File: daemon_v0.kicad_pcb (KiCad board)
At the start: 4 copper layers, 85.6 x 54 mm, 164 parts, among them J1 BATTERY JST, J10 WAGO 24V I/O, J11 AUX GPIO, J12 RADXA 40-PIN HEADER, J13 TRRS AUDIO, J14 SPEAKER, J2 USB-A ① (MALE), J3 USB-A ②, J4 USB-A ③, J5 SCREEN 8-PIN, J6 JOYSTICK 5-PIN, J7 PWR HDR, J8 USB-C GOOBAY, J9 RJ45 ETHERNET, Q1 PNP BC857, Q2 PMOS BSS84, Q3 NMOS 2N7002, Q4 IR DRIVE AO3400A, SW1 POWER BUTTON, U1 PMIC IP5328P, U10 ETH RTL8152B, U11 ISO ISO1212, U12 AMP MAX98357A, U13 MIC INMP441, U2 LDO 3.3V AP2112K, U3 HEARTBEAT NE555, U4 USB HUB SL2.1A, U5 STINGER 1 SY6280, U6 STINGER 2 SY6280, U7 STINGER 3 SY6280, U8 ADC ADS1015, U9 RF CC1101, Y1 12MHz, Y2 26MHz, Y3 25MHz

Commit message: feat: layout-ready board with Radxa reference, placement guide, and component grid
- Radxa Zero 3W outline drawn on User.Drawings (connectors, GPIO header, mounting holes)
- 55 key components staged in labeled grid (right of board) — drag onto board
- 109 passives hidden below board — follow parent ICs later
- docs/PLACEMENT_GUIDE.md: gamified step-by-step placement with separation rules
- docs/PLACEMENT_CONSTRAINTS.md: detailed A/B/C component classification
- docs/RADXA_REFERENCE.md: GPIO mapping, alignment, keep-out zones

Co-Authored-By: Claude Opus 4.6 <noreply@anthropic.com>
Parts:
- AE1: value 915MHz ANTENNA -> ANTENNA 915MHz
- C12: value 100u -> 100µF ELEC TIMER
- C7: value 100u -> 100µF TANT POWER TANK
- D1: value SS14 -> SS14 DIODE A
- D2: value SS14 -> SS14 DIODE B
- D3: value LED① -> WS2812B ①
- D4: value LED② -> WS2812B ②
- D5: value LED③ -> WS2812B ③
- D6: value LED④ -> WS2812B ④
- D7: value IR LED -> IR LED VSMB294008
- D8: value VCAN26A2 -> TVS ① VCAN26A2
- D9: value VCAN26A2 -> TVS ② VCAN26A2
- F1: value 60R -> PTC FUSE ①
- F2: value 60R -> PTC FUSE ②
- J12: value RADXA 40-PIN HEADER -> RADXA 40-PIN HDR
- J14: value SPEAKER -> SPEAKER JST
- J2: value USB-A ① (MALE) -> USB-A ① MALE
- J9: value RJ45 ETHERNET -> RJ45 MAGJACK
- L1: value 4.7µH BOOST -> 4.7µH BOOST IND
- Q1: value PNP BC857 -> BC857 PNP
- Q2: value PMOS BSS84 -> BSS84 PMOS
- Q3: value NMOS 2N7002 -> 2N7002 NMOS
- Q4: value IR DRIVE AO3400A -> AO3400A IR DRIVE
- TH1: value 10k -> NTC 10K (near U1!)
- U1: value PMIC IP5328P -> IP5328P PMIC
- U10: value ETH RTL8152B -> RTL8152B ETH PHY
- U11: value ISO ISO1212 -> ISO1212
- U12: value AMP MAX98357A -> MAX98357A AMP
- U13: value MIC INMP441 -> INMP441 MEMS MIC
- U2: value LDO 3.3V AP2112K -> AP2112K 3.3V LDO
- U3: value HEARTBEAT NE555 -> NE555 HEARTBEAT
- U4: value USB HUB SL2.1A -> SL2.1A USB HUB
- U5: value STINGER 1 SY6280 -> SY6280 ① (near J2)
- U6: value STINGER 2 SY6280 -> SY6280 ② (near J3)
- U7: value STINGER 3 SY6280 -> SY6280 ③ (near J4)
- U8: value ADC ADS1015 -> ADS1015 JOY ADC
- U9: value RF CC1101 -> CC1101 RF XCVR
- Y1: value 12MHz -> 12MHz XTAL (near U4)
- Y2: value 26MHz -> 26MHz XTAL (near U9)
- Y3: value 25MHz -> 25MHz XTAL (near U10)
- moved TP1 486.4 mm to (490.6, 95.0)
- moved TP2 484.1 mm to (490.6, 113.0)
- moved TP3 482.5 mm to (490.6, 131.0)
- moved TP4 481.7 mm to (490.6, 149.0)
- moved Q4 468.7 mm to (470.6, 149.0)
- moved Q3 466.6 mm to (470.6, 131.0)
- moved Q2 462.5 mm to (470.6, 113.0)
- moved Q1 461.0 mm to (470.6, 95.0)
- moved U8 447.3 mm to (450.6, 95.0)
- moved D6 435.2 mm to (430.6, 149.0)
- moved U3 433.0 mm to (450.6, 113.0)
- moved D5 430.8 mm to (430.6, 131.0)
- moved D4 427.0 mm to (430.6, 113.0)
- moved D3 424.2 mm to (430.6, 95.0)
- moved SW1 423.2 mm to (450.6, 131.0)
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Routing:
- removed copper zone on B.Cu, net (none)
- removed copper zone on F.Cu, net (none)
- removed copper zone on In1.Cu, net (none)
- removed copper zone on In2.Cu, net (none)
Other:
- board text added: "1"
- board text added: "40"
- board text added: "40-PIN GPIO HEADER"
- board text added: "54.0 mm"
- board text added: "Inductor↔XTALs ≥15mm | Antenna keepout 5mm | MagJack↔USB-C ≥15mm"
- board text added: "M2.5"
- board text added: "RADXA ZERO 3W (underneath)"
- board text added: "RULES: Power↔RF ≥20mm | Inductor↔RF ≥25mm | XTAL_26↔XTAL_25 ≥10mm"
- board text added: "SD"
- board text added: "SECONDARY COMPONENTS (109 passives) — don't touch, they follow their parent IC"
- board text added: "USB-C HOST"
- board text added: "USB-C OTG/PWR"
- board text added: "WiFi U.FL"
- board text added: "µHDMI"
- board text added: "← 85.6 mm →"
- board text added: "⚙️ INDUSTRIAL ISO"
- board text added: "⚠ NO TALL PARTS ON B.Cu IN THIS ZONE"
- board text added: "⚡ POWER"
- board text added: "🌐 ETHERNET"
- board text added: "🎮 CONTROL"
- board text added: "💡 LEDs + IR"
- board text added: "📍 TEST POINTS"
- board text added: "📡 RF (keep away from power!)"
- board text added: "🔀 USB HUB"
- board text added: "🔊 AUDIO"
- board text added: "🔌 CONNECTORS"
- board text added: "🔌 STINGER SWITCHES"
- board text added: "🔧 TRANSISTORS"

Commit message: fix: resolve hardware review blocker + warnings
BLOCKER B-1 FIXED:
- NE555 DIP-8 → NE555DR SOIC-8 (turnkey SMT compatible)
- 100µF electrolytic (THT, 8mm tall) → 100µF tantalum Case-D (SMD, 2.8mm)
- Eliminates all through-hole dependencies except RJ45 MagJack
- Resolves Z-height collision risk with Radxa stack

WARNING W-5 FIXED:
- C_TANT voltage rating 6.3V → 10V (2x derating on 5V rail)

HARDWARE REVIEW added (docs/HARDWARE_REVIEW.md):
- 1 blocker (now fixed), 11 warnings (quantified), 15 verified stable
- Power system, RF, audio, USB hub, Ethernet all verified stable
- Key remaining risks: WS2812B level (firmware open-drain), LDO thermal margin

Co-Authored-By: Claude Opus 4.6 <noreply@anthropic.com>
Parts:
- C12: footprint CP_Radial_D6.3mm_P2.50mm -> CP_EIA-7343-31_Kemet-D
- U3: footprint DIP-8_W7.62mm -> SOIC-8_3.9x4.9mm_P1.27mm

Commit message: fix: 40-pin header to female socket, add mic power LED, edge-mount power button
ECO #2026-03-HWR fixes:
- J12: PinHeader_2x20 → PinSocket_2x20 (female socket mates with Radxa male pins)
- SW1: PTS645 top-press → Alps SKRTLAE010 right-angle (flush with board edge)
- Added red 0402 LED + 1k resistor on INMP441 VDD (hardware mic-active indicator)
- Total components: 164 → 166 (mic LED + resistor added)
- All 164 tests pass

Co-Authored-By: Claude Opus 4.6 <noreply@anthropic.com>
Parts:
- added D12: RED_0402, LED_0402_1005Metric, F.Cu at (110.0, 184.0)
- added R45: 1k, R_0402_1005Metric, F.Cu at (125.0, 194.0)
- J12: footprint PinHeader_2x20_P2.54mm_Vertical -> PinSocket_2x20_P2.54mm_Vertical
- SW1: footprint SW_SPST_PTS645 -> SW_Push_1P1T-MP_NO_Horizontal_Alps_SKRTLAE010
- moved R22 95.1 mm to (100.0, 189.0)
- moved R40 95.1 mm to (100.0, 194.0)
- moved R5 10.0 mm to (130.0, 194.0)
- moved R6 10.0 mm to (135.0, 194.0)
- moved R7 10.0 mm to (140.0, 194.0)
- moved R8 10.0 mm to (145.0, 194.0)
- moved R9 10.0 mm to (150.0, 194.0)
- moved FB1 5.00 mm to (115.0, 184.0)
- moved FB2 5.00 mm to (120.0, 184.0)
- moved L2 5.00 mm to (125.0, 184.0)
- moved R1 5.00 mm to (130.0, 184.0)
- moved R10 5.00 mm to (135.0, 184.0)
- moved R11 5.00 mm to (140.0, 184.0)
- moved R12 5.00 mm to (145.0, 184.0)
- moved R13 5.00 mm to (150.0, 184.0)
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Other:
- board text added: "SECONDARY COMPONENTS (111 passives) — don't touch, they follow their parent IC"
- board text removed: "SECONDARY COMPONENTS (109 passives) — don't touch, they follow their parent IC"

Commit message: fix: netlist pad numbering + KiCad import with full net assignments
The netlist was outputting pin NAMES (CC1, VDD, EPAD, D+, etc.) but
KiCad footprints use pad NUMBERS (1, 2, 3...). Every IC had zero net
connections in KiCad because "CC1" != pad "2".

Added PIN_MAPS dict to gen_golden_netlist.py mapping pin names to KiCad
pad numbers for all 20+ IC/connector types (IP5328P QFN-40, SL2.1A,
RTL8152B, MAX98357A, CC1101, ISO1212, PCF8574, NE555, AP2112K, SY6280,
USB-C plug/receptacle, USB-A, TRRS jack, WS2812B, LEDs, MOSFETs, etc.)

Updated import_netlist.py to use .net file pad assignments directly
instead of trying to match pin names. Result: 802/802 pad-net
connections assigned (was 0).

Co-Authored-By: Claude Opus 4.6 (1M context) <noreply@anthropic.com>
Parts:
- removed AE1: ANTENNA 915MHz, Antenna_Chip_Johanson_0915AT43A0026
- removed D12: RED_0402, LED_0402_1005Metric
- removed J5: SCREEN 8-PIN, PinHeader_1x08_P2.54mm_Vertical
- removed TH1: NTC 10K (near U1!), R_0402_1005Metric
- added ANT1: 0915AT43A0026, Antenna_Chip_Johanson_0915AT43A0026, F.Cu at (280.0, 180.0)
- added BAT1: Li-ion, JST_PH_S2B-PH-K_1x02_P2.00mm_Horizontal, F.Cu at (220.0, 100.0)
- added C100: 100n, C_0402_1005Metric, F.Cu at (264.0, 468.0)
- added C101: 100n, C_0402_1005Metric, F.Cu at (272.0, 468.0)
- added C102: 100n, C_0402_1005Metric, F.Cu at (280.0, 468.0)
- added C103: 100n, C_0402_1005Metric, F.Cu at (288.0, 468.0)
- added C104: 100n, C_0402_1005Metric, F.Cu at (200.0, 476.0)
- added C63: 1p5, C_0402_1005Metric, F.Cu at (288.0, 428.0)
- added C64: 1p5, C_0402_1005Metric, F.Cu at (200.0, 436.0)
- added C65: 3p3, C_0402_1005Metric, F.Cu at (208.0, 436.0)
- added C66: 100p, C_0402_1005Metric, F.Cu at (216.0, 436.0)
- added C67: 12p, C_0402_1005Metric, F.Cu at (224.0, 436.0)
- added C68: 47p, C_0402_1005Metric, F.Cu at (232.0, 436.0)
- added C69: 10n, C_0402_1005Metric, F.Cu at (248.0, 436.0)
- added C70: 10n, C_0402_1005Metric, F.Cu at (272.0, 436.0)
- added C71: 10u, C_0805_2012Metric, F.Cu at (288.0, 436.0)
- added C72: 100n, C_0402_1005Metric, F.Cu at (200.0, 444.0)
- added C73: 100n, C_0402_1005Metric, F.Cu at (208.0, 444.0)
- added C74: 4u7, C_0402_1005Metric, F.Cu at (224.0, 444.0)
- added C75: 100n, C_0402_1005Metric, F.Cu at (232.0, 444.0)
- added C76: 4u7, C_0402_1005Metric, F.Cu at (240.0, 444.0)
- added C77: 100n, C_0402_1005Metric, F.Cu at (248.0, 444.0)
- added C78: 4u7, C_0402_1005Metric, F.Cu at (256.0, 444.0)
- added C79: 100n, C_0402_1005Metric, F.Cu at (264.0, 444.0)
- added C80: 4u7, C_0402_1005Metric, F.Cu at (272.0, 444.0)
- added C81: 100n, C_0402_1005Metric, F.Cu at (280.0, 444.0)
- added C82: 27p, C_0402_1005Metric, F.Cu at (288.0, 444.0)
- added C83: 27p, C_0402_1005Metric, F.Cu at (200.0, 452.0)
- added C84: 100n, C_0402_1005Metric, F.Cu at (216.0, 452.0)
- added C85: 100n, C_0402_1005Metric, F.Cu at (224.0, 452.0)
- added C86: 10u, C_0805_2012Metric, F.Cu at (232.0, 452.0)
- added C87: 100n, C_0402_1005Metric, F.Cu at (240.0, 452.0)
- added C88: 100n, C_0402_1005Metric, F.Cu at (248.0, 452.0)
- added C89: 100n, C_0402_1005Metric, F.Cu at (208.0, 460.0)
- added C90: 100n, C_0402_1005Metric, F.Cu at (224.0, 460.0)
- added C91: 100n, C_0402_1005Metric, F.Cu at (232.0, 460.0)
- added C92: 100n, C_0402_1005Metric, F.Cu at (240.0, 460.0)
- added C93: 100n, C_0402_1005Metric, F.Cu at (248.0, 460.0)
- added C94: 100n, C_0402_1005Metric, F.Cu at (256.0, 460.0)
- added C95: 10u, C_0805_2012Metric, F.Cu at (280.0, 460.0)
- added C96: 100n, C_0402_1005Metric, F.Cu at (288.0, 460.0)
- added C97: 10u, C_0805_2012Metric, F.Cu at (200.0, 468.0)
- added C98: 1n, C_0402_1005Metric, F.Cu at (240.0, 468.0)
- added C99: 1n, C_0402_1005Metric, F.Cu at (248.0, 468.0)
- added J15: SJ2-2531X, Jack_3.5mm_SJ2-2531X-SMT, F.Cu at (280.0, 240.0)
- added J16: Speaker, JST_SH_SM02B-SRSS-TB_1x02-1MP_P1.00mm_Horizontal, F.Cu at (200.0, 260.0)
- added L3: 12n, L_0402_1005Metric, F.Cu at (260.0, 314.0)
- added L4: 18n, L_0402_1005Metric, F.Cu at (272.0, 314.0)
- added L5: 18n, L_0402_1005Metric, F.Cu at (284.0, 314.0)
- added L6: 12n, L_0402_1005Metric, F.Cu at (200.0, 326.0)
- added L7: 12n, L_0402_1005Metric, F.Cu at (212.0, 326.0)
- added L8: 3n3, L_0402_1005Metric, F.Cu at (224.0, 326.0)
- added LED1: WS2812B-2020, LED_WS2812B-2020_PLCC4_2.0x2.0mm, F.Cu at (224.0, 338.0)
- added LED2: WS2812B-2020, LED_WS2812B-2020_PLCC4_2.0x2.0mm, F.Cu at (236.0, 338.0)
- added LED3: WS2812B-2020, LED_WS2812B-2020_PLCC4_2.0x2.0mm, F.Cu at (248.0, 338.0)
- added LED4: WS2812B-2020, LED_WS2812B-2020_PLCC4_2.0x2.0mm, F.Cu at (260.0, 338.0)
- added LED5: VSMB294008, LED_0603_1608Metric_Pad1.05x0.95mm_HandSolder, F.Cu at (272.0, 338.0)
- added LED6: RED_0402, LED_0402_1005Metric, F.Cu at (224.0, 350.0)
- added LED7: RED_0402, LED_0402_1005Metric, F.Cu at (236.0, 350.0)
- added LED8: GREEN_0402, LED_0402_1005Metric, F.Cu at (248.0, 350.0)
- added R46: 10k, R_0402_1005Metric, F.Cu at (216.0, 460.0)
- added R47: 100, R_1206_3216Metric, F.Cu at (264.0, 460.0)
- added R48: 100k, R_0402_1005Metric, F.Cu at (272.0, 460.0)
- added R49: 100k, R_0402_1005Metric, F.Cu at (208.0, 468.0)
- added R50: 47k, R_0402_1005Metric, F.Cu at (216.0, 468.0)
- added R51: 10R, R_0805_2012Metric, F.Cu at (224.0, 468.0)
- added R52: 10R, R_0805_2012Metric, F.Cu at (232.0, 468.0)
- added R53: 10k, R_0402_1005Metric, F.Cu at (256.0, 468.0)
- added R54: 1k, R_0402_1005Metric, F.Cu at (208.0, 476.0)
- added R55: 1k, R_0402_1005Metric, F.Cu at (216.0, 476.0)
- added REF_Radxa_Zero_3W_Reference: Radxa_Zero_3W, Radxa_Zero_3W_Reference, F.Cu at (50.0, 50.0)
- added REF_Speaker_Oval_Reference: Speaker_Oval_20x14mm, Speaker_Oval_Reference, F.Cu at (50.0, 120.0)
- added SW2: SKRHABE010, SW_Alps_SKRHABE010, F.Cu at (212.0, 338.0)
- added U14: SL2.1A, SOIC-16_3.9x9.9mm_P1.27mm, F.Cu at (220.0, 120.0)
- added U15: SY6280AAC, SOT-23-5, F.Cu at (220.0, 160.0)
- added U16: USBLC6-2SC6, SOT-23-6, F.Cu at (240.0, 140.0)
- added U17: USBLC6-2SC6, SOT-23-6, F.Cu at (200.0, 160.0)
- added U18: USBLC6-2SC6, SOT-23-6, F.Cu at (260.0, 160.0)
- added U19: USBLC6-2SC6, SOT-23-6, F.Cu at (220.0, 180.0)
- added U20: USBLC6-2SC6, SOT-23-6, F.Cu at (260.0, 200.0)
- added U21: PCF8574, SOIC-16_3.9x9.9mm_P1.27mm, F.Cu at (240.0, 220.0)
- added U22: SY6280AAC, SOT-23-5, F.Cu at (280.0, 160.0)
- added U23: 74AHCT1G125, SOT-23-5, F.Cu at (260.0, 220.0)
- added U24: INMP441, InvenSense_INMP441_BottomPort, F.Cu at (260.0, 240.0)
- added U25: ESD9B5.0ST5G, SOT-323_SC-70, F.Cu at (220.0, 260.0)
- added U26: ESD9B5.0ST5G, SOT-323_SC-70, F.Cu at (240.0, 260.0)
- added Y4: 25MHz, Crystal_SMD_3225-4Pin_3.2x2.5mm, F.Cu at (200.0, 338.0)
- C1, C10, C21, C23, C27, C29, C3: value 10u -> 100n; footprint C_0805_2012Metric -> C_0402_1005Metric
- C12: value 100µF ELEC TIMER -> 4u7; footprint CP_EIA-7343-31_Kemet-D -> C_0402_1005Metric
- C13, C51: value 10n -> 100u; footprint C_0402_1005Metric -> CP_EIA-7343-31_Kemet-D
- C14, C34, C42: value 22p -> 10u; footprint C_0402_1005Metric -> C_0805_2012Metric
- C15, C35, C43: value 22p -> 100n
- C18, C24: value 100n -> 22p
- C19, C25: value 10u -> 22p; footprint C_0805_2012Metric -> C_0402_1005Metric
- C2, C20, C26, C30, C32, C36, C38, C4, C44, C48: value 100n -> 10u; footprint C_0402_1005Metric -> C_0805_2012Metric
- C39: value 0.5p -> 100n
- C40: value 4.7p -> 10u; footprint C_0402_1005Metric -> C_0805_2012Metric
- C41: value 1p -> 100n
- C5: value 22u -> 100n; footprint C_0805_2012Metric -> C_0402_1005Metric
- C53: value 10u -> 27p; footprint C_0805_2012Metric -> C_0402_1005Metric
- C54: value 100n -> 27p
- C57: value 0.1uF -> 100n
- C58, C59, C60: value 0.1uF -> 100p
- C6: value 100n -> 22u; footprint C_0402_1005Metric -> C_0805_2012Metric
- C61: value 1n -> 100p
- C62: value 1n -> 1p0
- C7: value 100µF TANT POWER TANK -> 100n; footprint CP_EIA-3528-21_Kemet-B -> C_0402_1005Metric
- D1: value SS14 DIODE A -> SMBJ5.0A; footprint D_SMA -> D_SMB
- D10, D11: value ESD9B5.0ST5G -> ESD5Z3.3; footprint SOT-323_SC-70 -> D_SOD-523
- D2: value SS14 DIODE B -> SMBJ5.0A; footprint D_SMA -> D_SMB
- D3: value WS2812B ① -> ESD5Z3.3; footprint LED_WS2812B_PLCC4_5.0x5.0mm_P3.2mm -> D_SOD-523
- D4: value WS2812B ② -> ESD5Z3.3; footprint LED_WS2812B_PLCC4_5.0x5.0mm_P3.2mm -> D_SOD-523
- D5: value WS2812B ③ -> ESD5Z3.3; footprint LED_WS2812B_PLCC4_5.0x5.0mm_P3.2mm -> D_SOD-523
- D6: value WS2812B ④ -> SS34; footprint LED_WS2812B_PLCC4_5.0x5.0mm_P3.2mm -> D_SMA
- D7: value IR LED VSMB294008 -> SS34; footprint LED_0603_1608Metric_Pad1.05x0.95mm_HandSolder -> D_SMA
- D8: value TVS ① VCAN26A2 -> SS34; footprint D_SMB -> D_SMA
- D9: value TVS ② VCAN26A2 -> VCAN26A2; footprint D_SMB -> SOT-323_SC-70
- F1: value PTC FUSE ① -> 60R
- F2: value PTC FUSE ② -> 60R
- FB1: value BLM18AG601SN1 -> BLM31PG601SN1L; footprint L_0402_1005Metric -> L_1206_3216Metric
- FB2: footprint L_0402_1005Metric -> L_0603_1608Metric
- J1: value BATTERY JST -> PTC_2A; footprint JST_PH_S2B-PH-K_1x02_P2.00mm_Horizontal -> R_1210_3225Metric
- J10: value WAGO 24V I/O -> USB_A; footprint TerminalBlock_WAGO_2060-404_1x04_P4.00mm_Horizontal -> USB_A_CNCTech_1001-011-01101_Horizontal
- J11: value AUX GPIO -> USB_C_Receptacle; footprint PinHeader_1x04_P2.54mm_Vertical -> USB_C_Receptacle_HRO_TYPE-C-31-M-12
- J12: value RADXA 40-PIN HDR -> WAGO-2060-404; footprint PinSocket_2x20_P2.54mm_Vertical -> TerminalBlock_WAGO_2060-404_1x04_P4.00mm_Horizontal
- J13: value TRRS AUDIO -> Goobay-74446; footprint Jack_3.5mm_SJ2-2531X-SMT -> USB_C_Receptacle_HRO_TYPE-C-31-M-12
- J14: value SPEAKER JST -> HR911105A; footprint JST_SH_SM02B-SRSS-TB_1x02-1MP_P1.00mm_Horizontal -> RJ45_Hanrun_HR911105A_Horizontal
- J2: value USB-A ① MALE -> 10m; footprint USB_A_CNCTech_1001-011-01101_Horizontal -> R_1210_3225Metric
- J3: value USB-A ② -> Radxa-40Pin; footprint USB_A_Molex_67643_Horizontal -> PinSocket_2x20_P2.54mm_Vertical
- J4: value USB-A ③ -> AUX-GPIO; footprint USB_A_Molex_67643_Horizontal -> PinSocket_2x04_P2.54mm_Vertical
- J6: value JOYSTICK 5-PIN -> ST7789V2; footprint PinHeader_1x05_P2.54mm_Vertical -> PinSocket_1x08_P2.54mm_Vertical
- J7: value PWR HDR -> USB_C_Plug_USB2.0; footprint PinHeader_1x03_P2.54mm_Vertical -> USB_C_Plug_GCT_USB4155
- J8: value USB-C GOOBAY -> USB_A; footprint USB_C_Receptacle_HRO_TYPE-C-31-M-12 -> USB_A_Molex_67643_Horizontal
- J9: value RJ45 MAGJACK -> USB_A; footprint RJ45_Hanrun_HR911105A_Horizontal -> USB_A_Molex_67643_Horizontal
- L1: value 4.7µH BOOST IND -> 2u2
- L2: value 10n -> 12n
- Q1: value BC857 PNP -> BC857
- Q2: value BSS84 PMOS -> BSS84
- Q3: value 2N7002 NMOS -> 2N7002
- Q4: value AO3400A IR DRIVE -> AO3400A
- R1: value 0 -> 100k; footprint R_1210_3225Metric -> R_0402_1005Metric
- R10: value 12k -> 470
- R13, R14: value 10k -> 15k
- R15: value 10k -> 12k
- R17: value 10k -> 3.3k
- R19, R21, R27: value 10k -> 13k
- R2: value 0 -> 10k; footprint R_1210_3225Metric -> R_0402_1005Metric
- R20, R26: value 13k -> 10k
- R24, R25: value 10k -> 56k
- R28: value 430k -> 47k
- R29: value 620k -> 150
- R30: value 100k -> 10k
- R31: value 10k -> 82; footprint R_0402_1005Metric -> R_0805_2012Metric
- R32: value 5k1 -> 56k
- R33: value 5k1 -> 10k
- R34: value 0 -> 562; footprint R_0402_1005Metric -> R_2512_6332Metric
- R35: value 0 -> 562
- R36: value 1k -> 562; footprint R_0402_1005Metric -> R_2512_6332Metric
- R37: value 33 -> 562
- R38: value 562 -> 12.1k
- R39: value 562 -> 10k
- R4, R5: value 470 -> 100k
- R40, R41, R45: value 1k -> 10k
- R42: value 633k -> 10k
- R6: value 220k -> 51k
- R7: value 150 -> 4.7k
- R8: value 10k -> 4.7k
- R9: value 82 -> 470
- SW1: value POWER BUTTON -> SW_PWR
- TP1: value TP VIN -> TP_VIN
- TP2: value TP BAT -> TP_BAT
- TP3: value TP SW -> TP_LX
- TP4: value TP VOUT -> TP_VSYS
- U1: value IP5328P PMIC -> IP5328P
- U10: value RTL8152B ETH PHY -> MAX98357A; footprint QFN-32-1EP_5x5mm_P0.5mm_EP3.1x3.1mm -> QFN-16-1EP_3x3mm_P0.5mm_EP1.75x1.75mm
- U11: footprint SOIC-16W_7.5x10.3mm_P1.27mm -> SSOP-16_3.9x4.9mm_P0.635mm
- U12: value MAX98357A AMP -> USBLC6-2SC6; footprint QFN-16-1EP_3x3mm_P0.5mm_EP1.75x1.75mm -> SOT-23-6
- U13: value INMP441 MEMS MIC -> INMP441
- U2: value AP2112K 3.3V LDO -> AP2112K-3.3
- U3: value NE555 HEARTBEAT -> SL2.1A; footprint SOIC-8_3.9x4.9mm_P1.27mm -> SOIC-16_3.9x9.9mm_P1.27mm
- U4: value SL2.1A USB HUB -> SY6280AAAC; footprint QFN-28-1EP_5x5mm_P0.5mm_EP3.35x3.35mm -> SOT-23-5
- U5: value SY6280 ① (near J2) -> SY6280AAC
- U6: value SY6280 ② (near J3) -> SY6280AAC
- U7: value SY6280 ③ (near J4) -> NE555DR; footprint SOT-23-5 -> SOIC-8_3.9x4.9mm_P1.27mm
- U8: value ADS1015 JOY ADC -> CC1101; footprint VSSOP-10_3x3mm_P0.5mm -> QFN-20-1EP_4x4mm_P0.5mm_EP2.6x2.6mm
- U9: value CC1101 RF XCVR -> RTL8152B; footprint QFN-20-1EP_4x4mm_P0.5mm_EP2.6x2.6mm -> QFN-24-1EP_4x4mm_P0.5mm_EP2.6x2.6mm
- Y1: value 12MHz XTAL (near U4) -> 12MHz
- Y2: value 26MHz XTAL (near U9) -> 12MHz
- Y3: value 25MHz XTAL (near U10) -> 27MHz
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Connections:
- C1 pad 1: (no net) -> IP5328P_BST
- C1 pad 2: (no net) -> LX
- C10 pad 1: (no net) -> IP5328P_VBUSG
- C10 pad 2: (no net) -> GND
- C11 pad 1: (no net) -> IP5328P_VING
- C11 pad 2: (no net) -> GND
- C12 pad 1: (no net) -> IP5328P_VREG
- C12 pad 2: (no net) -> GND
- C13 pad 1: (no net) -> 5V_SYS
- C13 pad 2: (no net) -> GND
- C14 pad 1: (no net) -> 5V_SYS
- C14 pad 2: (no net) -> GND
- C15 pad 1: (no net) -> 5V_SYS
- C15 pad 2: (no net) -> GND
- C16 pad 1: (no net) -> 3V3_CLEAN
- C16 pad 2: (no net) -> GND
- C17 pad 1: (no net) -> 3V3_CLEAN
- C17 pad 2: (no net) -> GND
- C18 pad 1: (no net) -> HUB1_XI
- C18 pad 2: (no net) -> GND
- C19 pad 1: (no net) -> HUB1_XO
- C19 pad 2: (no net) -> GND
- C2 pad 1: (no net) -> VIN
- C2 pad 2: (no net) -> GND
- C20 pad 1: (no net) -> 5V_SYS
- C20 pad 2: (no net) -> GND
- C21 pad 1: (no net) -> 5V_SYS
- C21 pad 2: (no net) -> GND
- C22 pad 1: (no net) -> HUB1_VDD33
- C22 pad 2: (no net) -> GND
- C23 pad 1: (no net) -> HUB1_VDD18
- C23 pad 2: (no net) -> GND
- C24 pad 1: (no net) -> HUB2_XI
- C24 pad 2: (no net) -> GND
- C25 pad 1: (no net) -> HUB2_XO
- C25 pad 2: (no net) -> GND
- C26 pad 1: (no net) -> 5V_SYS
- C26 pad 2: (no net) -> GND
- C27 pad 1: (no net) -> 5V_SYS
- C27 pad 2: (no net) -> GND
- C28 pad 1: (no net) -> HUB2_VDD33
- C28 pad 2: (no net) -> GND
- C29 pad 1: (no net) -> HUB2_VDD18
- C29 pad 2: (no net) -> GND
- C3 pad 1: (no net) -> VIN
- C3 pad 2: (no net) -> GND
- C30 pad 1: (no net) -> 5V_SYS
- C30 pad 2: (no net) -> GND
- C31 pad 1: (no net) -> 5V_SYS
- C31 pad 2: (no net) -> GND
- C32 pad 1: (no net) -> USB_VBUS_1
- C32 pad 2: (no net) -> GND
- C33 pad 1: (no net) -> USB_VBUS_1
- C33 pad 2: (no net) -> GND
- C34 pad 1: (no net) -> 5V_SYS
- C34 pad 2: (no net) -> GND
- C35 pad 1: (no net) -> 5V_SYS
- C35 pad 2: (no net) -> GND
- C36 pad 1: (no net) -> USB_VBUS_2
- C36 pad 2: (no net) -> GND
- C37 pad 1: (no net) -> USB_VBUS_2
- C37 pad 2: (no net) -> GND
- C38 pad 1: (no net) -> 5V_SYS
- C38 pad 2: (no net) -> GND
- C39 pad 1: (no net) -> 5V_SYS
- C39 pad 2: (no net) -> GND
- C4 pad 1: (no net) -> BAT
- C4 pad 2: (no net) -> GND
- C40 pad 1: (no net) -> USB_VBUS_3
- C40 pad 2: (no net) -> GND
- C41 pad 1: (no net) -> USB_VBUS_3
- C41 pad 2: (no net) -> GND
- C42 pad 1: (no net) -> 5V_SYS
- C42 pad 2: (no net) -> GND
- C43 pad 1: (no net) -> 5V_SYS
- C43 pad 2: (no net) -> GND
- C44 pad 1: (no net) -> USB_VBUS_4
- C44 pad 2: (no net) -> GND
- C45 pad 1: (no net) -> USB_VBUS_4
- C45 pad 2: (no net) -> GND
- C46 pad 1: (no net) -> 5V_SYS
- C46 pad 2: (no net) -> GND
- C47 pad 1: (no net) -> 5V_SYS
- C47 pad 2: (no net) -> GND
- C48 pad 1: (no net) -> USB_VBUS_5
- C48 pad 2: (no net) -> GND
- C49 pad 1: (no net) -> USB_VBUS_5
- C49 pad 2: (no net) -> GND
- C5 pad 1: (no net) -> BAT
- C5 pad 2: (no net) -> GND
- C50 pad 1: (no net) -> 5V_SYS
- C50 pad 2: (no net) -> GND
- C51 pad 1: (no net) -> HB_TMR_THR
- C51 pad 2: (no net) -> GND
- C52 pad 1: (no net) -> HB_TMR_CTRL
- C52 pad 2: (no net) -> GND
- C53 pad 1: (no net) -> RF_XI
- C53 pad 2: (no net) -> GND
- C54 pad 1: (no net) -> RF_XO
- C54 pad 2: (no net) -> GND
- C55 pad 1: (no net) -> RF_DCOUPL
- C55 pad 2: (no net) -> GND
- C56 pad 1: (no net) -> 3V3_CLEAN
- C56 pad 2: (no net) -> GND
- C57 pad 1: (no net) -> 3V3_CLEAN
- C57 pad 2: (no net) -> GND
- C58 pad 1: (no net) -> 3V3_CLEAN
- C58 pad 2: (no net) -> GND
- C59 pad 1: (no net) -> 3V3_CLEAN
- C59 pad 2: (no net) -> GND
- C6 pad 1: (no net) -> IP5328P_VSYS
- C6 pad 2: (no net) -> GND
- C60 pad 1: (no net) -> 3V3_CLEAN
- C60 pad 2: (no net) -> GND
- C61 pad 1: (no net) -> 3V3_CLEAN
- C61 pad 2: (no net) -> GND
- C62 pad 1: (no net) -> RF_BAL_P
- C62 pad 2: (no net) -> GND
- C7 pad 1: (no net) -> IP5328P_VSYS
- C7 pad 2: (no net) -> GND
- C8 pad 1: (no net) -> IP5328P_VBUS
- C8 pad 2: (no net) -> GND
- C9 pad 1: (no net) -> IP5328P_VBUS
- C9 pad 2: (no net) -> GND
- D1 pad 1: (no net) -> GND
- D1 pad 2: (no net) -> VIN
- D10 pad 1: (no net) -> GND
- D10 pad 2: (no net) -> GOOBAY_CC1
- D11 pad 1: (no net) -> GND
- D11 pad 2: (no net) -> GOOBAY_CC2
- D2 pad 1: (no net) -> GND
- D2 pad 2: (no net) -> 5V_SYS
- D3 pad 1: (no net) -> GND
- D3 pad 2: (no net) -> STINGER1_CC
- D4 pad 1: (no net) -> GND
- D4 pad 2: (no net) -> STINGER5_CC1
- D5 pad 1: (no net) -> GND
- D5 pad 2: (no net) -> STINGER5_CC2
- D6 pad 1: (no net) -> USB_VBUS_1
- D6 pad 2: (no net) -> VIN
- D7 pad 1: (no net) -> USB_VBUS_4
- D7 pad 2: (no net) -> VIN
- D8 pad 1: (no net) -> USB_VBUS_5
- D8 pad 2: (no net) -> VIN
- D9 pad 1: (no net) -> ISO_IN1_PTCA
- D9 pad 2: (no net) -> ISO_GND1
- F1 pad 1: (no net) -> ISO_IN1_RAW
- F1 pad 2: (no net) -> ISO_IN1_PTCA
- F2 pad 1: (no net) -> ISO_IN2_RAW
- F2 pad 2: (no net) -> ISO_IN2_PTCA
- FB1 pad 1: (no net) -> 5V_SYS
- FB1 pad 2: (no net) -> 5V_AUDIO
- FB2 pad 1: (no net) -> 3V3_SYS
- FB2 pad 2: (no net) -> MIC_VDD
- J1 pad 1: (no net) -> BAT
- J1 pad 2: (no net) -> BAT_ISO
- J10 pad 1: (no net) -> USB_VBUS_4
- J10 pad 2: (no net) -> HUB2_DN_DM_1
- J10 pad 3: (no net) -> HUB2_DN_DP_1
- J10 pad 4: (no net) -> GND
- J12 pad 1: (no net) -> ISO_GND1
- J12 pad 2: (no net) -> ISO_VCC1
- J12 pad 3: (no net) -> ISO_IN1_RAW
- J12 pad 4: (no net) -> ISO_IN2_RAW
- J14 pad 1: (no net) -> ETH_MDI_TXP
- J14 pad 2: (no net) -> ETH_MDI_TXN
- J2 pad 1: (no net) -> IP5328P_VSYS
- J2 pad 2: (no net) -> 5V_SYS
- J3 pad 1: (no net) -> 3V3_SYS
- J3 pad 2: (no net) -> RADXA_GPIO_5V
- J3 pad 3: (no net) -> I2C1_SDA
- J3 pad 4: (no net) -> RADXA_GPIO_5V
- J3 pad 5: (no net) -> I2C1_SCL
- J4 pad 1: (no net) -> ISO_DO1
- J4 pad 2: (no net) -> ISO_DO2
- J4 pad 3: (no net) -> IR_GPIO
- J4 pad 4: (no net) -> AUX_GPIO_1
- J4 pad 5: (no net) -> AUX_GPIO_2
- J6 pad 1: (no net) -> GND
- J6 pad 2: (no net) -> 3V3_SYS
- J6 pad 3: (no net) -> SPI3_CLK
- J6 pad 4: (no net) -> SPI3_MOSI
- J6 pad 5: (no net) -> SCREEN_RST
- J9 pad 1: (no net) -> USB_VBUS_3
- J9 pad 2: (no net) -> HUB1_DN_DM_3
- J9 pad 3: (no net) -> HUB1_DN_DP_3
- J9 pad 4: (no net) -> GND
- L1 pad 1: (no net) -> LX
- L1 pad 2: (no net) -> BAT_ISO
- L2 pad 1: (no net) -> RF_ANT_P
- L2 pad 2: (no net) -> RF_BAL_P
- Q1 pad 1: (no net) -> 5V_SYS
- Q1 pad 2: (no net) -> BJT_BASE
- Q1 pad 3: (no net) -> BJT_COLLECTOR
- Q2 pad 1: (no net) -> 5V_SYS
- Q2 pad 2: (no net) -> PMIC_KEY
- Q2 pad 3: (no net) -> NAV_CENTER
- Q3 pad 1: (no net) -> PMIC_KILL
- Q3 pad 2: (no net) -> PMIC_KEY
- Q3 pad 3: (no net) -> GND
- Q4 pad 1: (no net) -> IR_GPIO
- Q4 pad 2: (no net) -> IR_LED_N
- Q4 pad 3: (no net) -> GND
- R1 pad 1: (no net) -> VIN
- R1 pad 2: (no net) -> GND
- R10 pad 1: (no net) -> I2C1_SCL
- R10 pad 2: (no net) -> I2C1_PMIC_SCL
- R11 pad 1: (no net) -> 5V_SYS
- R11 pad 2: (no net) -> GND
- R12 pad 1: (no net) -> PMIC_KILL
- R12 pad 2: (no net) -> GND
- R13 pad 1: (no net) -> HUB2_DN_DP_4
- R13 pad 2: (no net) -> GND
- R14 pad 1: (no net) -> HUB2_DN_DM_4
- R14 pad 2: (no net) -> GND
- R15 pad 1: (no net) -> 5V_SYS
- R15 pad 2: (no net) -> STINGER1_CC
- R16 pad 1: (no net) -> 5V_SYS
- R16 pad 2: (no net) -> STINGER_EN_1
- R17 pad 1: (no net) -> STINGER_ISET_1
- R17 pad 2: (no net) -> GND
- R18 pad 1: (no net) -> 3V3_SYS
- R18 pad 2: (no net) -> STINGER_EN_2
- R19 pad 1: (no net) -> STINGER_ISET_2
- R19 pad 2: (no net) -> GND
- R2 pad 1: (no net) -> IP5328P_RSET
- R2 pad 2: (no net) -> GND
- R20 pad 1: (no net) -> 3V3_SYS
- R20 pad 2: (no net) -> STINGER_EN_3
- R21 pad 1: (no net) -> STINGER_ISET_3
- R21 pad 2: (no net) -> GND
- R22 pad 1: (no net) -> 3V3_SYS
- R22 pad 2: (no net) -> STINGER_EN_4
- R23 pad 1: (no net) -> STINGER_ISET_4
- R23 pad 2: (no net) -> GND
- R24 pad 1: (no net) -> 3V3_SYS
- R24 pad 2: (no net) -> STINGER5_CC1
- R25 pad 1: (no net) -> 3V3_SYS
- R25 pad 2: (no net) -> STINGER5_CC2
- R26 pad 1: (no net) -> 3V3_SYS
- R26 pad 2: (no net) -> STINGER_EN_5
- R27 pad 1: (no net) -> STINGER_ISET_5
- R27 pad 2: (no net) -> GND
- R28 pad 1: (no net) -> 5V_SYS
- R28 pad 2: (no net) -> HB_TMR_NODE_A
- R29 pad 1: (no net) -> HB_TMR_NODE_A
- R29 pad 2: (no net) -> HB_TMR_THR
- R3 pad 1: (no net) -> IP5328P_LIGHT
- R3 pad 2: (no net) -> GND
- R30 pad 1: (no net) -> HB_TMR_OUT
- R30 pad 2: (no net) -> BJT_BASE
- R31 pad 1: (no net) -> BJT_COLLECTOR
- R31 pad 2: (no net) -> GND
- R32 pad 1: (no net) -> RF_RBIAS
- R32 pad 2: (no net) -> GND
- R33 pad 1: (no net) -> 3V3_CLEAN
- R33 pad 2: (no net) -> RF_CS_N
- R34 pad 1: (no net) -> ISO_IN1_PTCA
- R34 pad 2: (no net) -> ISO_IN1
- R35 pad 1: (no net) -> ISO_SENSE1
- R35 pad 2: (no net) -> ISO_GND1
- R36 pad 1: (no net) -> ISO_IN2_PTCA
- R36 pad 2: (no net) -> ISO_IN2
- R37 pad 1: (no net) -> ISO_SENSE2
- R37 pad 2: (no net) -> ISO_GND1
- R38 pad 1: (no net) -> RTL_RSET
- R38 pad 2: (no net) -> GND
- R39 pad 1: (no net) -> 3V3_CLEAN
- R39 pad 2: (no net) -> RTL_LANWAKEB
- R4 pad 1: (no net) -> IP5328P_VOUT1G
- R4 pad 2: (no net) -> GND
- R40 pad 1: (no net) -> 3V3_SYS
- R40 pad 2: (no net) -> SPI3_CS
- R41 pad 1: (no net) -> 3V3_SYS
- R41 pad 2: (no net) -> NAV_UP
- R42 pad 1: (no net) -> 3V3_SYS
- R42 pad 2: (no net) -> NAV_DOWN
- R43 pad 1: (no net) -> 3V3_SYS
- R43 pad 2: (no net) -> NAV_LEFT
- R44 pad 1: (no net) -> 3V3_SYS
- R44 pad 2: (no net) -> NAV_RIGHT
- R45 pad 1: (no net) -> 3V3_SYS
- R45 pad 2: (no net) -> NAV_CENTER
- R5 pad 1: (no net) -> IP5328P_VOUT2G
- R5 pad 2: (no net) -> GND
- R6 pad 1: (no net) -> IP5328P_NTC
- R6 pad 2: (no net) -> GND
- R7 pad 1: (no net) -> 3V3_SYS
- R7 pad 2: (no net) -> I2C1_SDA
- R8 pad 1: (no net) -> 3V3_SYS
- R8 pad 2: (no net) -> I2C1_SCL
- R9 pad 1: (no net) -> I2C1_SDA
- R9 pad 2: (no net) -> I2C1_PMIC_SDA
- SW1 pad 1: (no net) -> PMIC_KEY
- SW1 pad 2: (no net) -> GND
- TP1 pad 1: (no net) -> VIN
- TP2 pad 1: (no net) -> BAT
- TP3 pad 1: (no net) -> LX
- TP4 pad 1: (no net) -> IP5328P_VSYS
- U1 pad 1: (no net) -> GND
- U1 pad 10: (no net) -> IP5328P_NTC
- U1 pad 11: (no net) -> I2C1_PMIC_SCL
- U1 pad 12: (no net) -> I2C1_PMIC_SDA
- U1 pad 13: (no net) -> IP5328P_VSET
- U1 pad 14: (no net) -> LX
- U1 pad 15: (no net) -> LX
- U1 pad 16: (no net) -> LX
- U1 pad 17: (no net) -> LX
- U1 pad 18: (no net) -> LX
- U1 pad 19: (no net) -> IP5328P_BST
- U1 pad 2: (no net) -> GOOBAY_CC1
- U1 pad 20: (no net) -> IP5328P_LIGHT
- U1 pad 21: (no net) -> IP5328P_RSET
- U1 pad 22: (no net) -> IP5328P_VSYS
- U1 pad 23: (no net) -> IP5328P_VSYS
- U1 pad 24: (no net) -> IP5328P_VSYS
- U1 pad 25: (no net) -> 5V_SYS
- U1 pad 26: (no net) -> PMIC_KEY
- U1 pad 27: (no net) -> IP5328P_VREG
- U1 pad 28: (no net) -> BAT_ISO
- U1 pad 29: (no net) -> GND
- U1 pad 3: (no net) -> GOOBAY_CC2
- U1 pad 30: (no net) -> VIN
- U1 pad 31: (no net) -> IP5328P_VING
- U1 pad 32: (no net) -> IP5328P_VBUS
- U1 pad 33: (no net) -> IP5328P_VBUSG
- U1 pad 34: (no net) -> IP5328P_VSYS
- U1 pad 35: (no net) -> IP5328P_VOUT2G
- U1 pad 36: (no net) -> IP5328P_VOUT1G
- U1 pad 37: (no net) -> IP5328P_VSYS
- U1 pad 38: (no net) -> GND
- U1 pad 39: (no net) -> GND
- U1 pad 4: (no net) -> GND
- U1 pad 40: (no net) -> GND
- U1 pad 41: (no net) -> GND
- U1 pad 5: (no net) -> GND
- U1 pad 6: (no net) -> GND
- U1 pad 7: (no net) -> GND
- U1 pad 8: (no net) -> IP5328P_VSYS
- U1 pad 9: (no net) -> IP5328P_VSYS
- U10 pad 1: (no net) -> 5V_AUDIO
- U10 pad 10: (no net) -> GND
- U10 pad 11: (no net) -> GND
- U10 pad 12: (no net) -> GND
- U10 pad 13: (no net) -> AMP_OUT_N
- U10 pad 14: (no net) -> GND
- U10 pad 15: (no net) -> AMP_OUT_P
- U10 pad 16: (no net) -> GND
- U10 pad 17: (no net) -> GND
- U10 pad 2: (no net) -> GND
- U10 pad 3: (no net) -> AMP_SD
- U10 pad 4: (no net) -> GND
- U10 pad 5: (no net) -> GND
- U10 pad 6: (no net) -> I2S_DATA_OUT
- U10 pad 7: (no net) -> I2S_BCLK
- U10 pad 8: (no net) -> I2S_LRCLK
- U10 pad 9: (no net) -> GND
- U11 pad 1: (no net) -> 3V3_SYS
- U11 pad 10: (no net) -> ISO_SENSE2
- U11 pad 11: (no net) -> ISO_IN2
- U11 pad 12: (no net) -> ISO_GND1
- U11 pad 13: (no net) -> ISO_SENSE1
- U11 pad 14: (no net) -> ISO_IN1
- U11 pad 15: (no net) -> NC
- U11 pad 16: (no net) -> NC
- U11 pad 2: (no net) -> ISO_DO1
- U11 pad 3: (no net) -> ISO_DO2
- U11 pad 4: (no net) -> 3V3_SYS
- U11 pad 5: (no net) -> GND
- U11 pad 6: (no net) -> ISO_SUB1
- U11 pad 7: (no net) -> NC
- U11 pad 8: (no net) -> ISO_SUB2
- U11 pad 9: (no net) -> ISO_GND1
- U12 pad 1: (no net) -> HUB1_DN_DM_1
- U12 pad 2: (no net) -> GND
- U12 pad 3: (no net) -> HUB1_DN_DM_1
- U12 pad 4: (no net) -> HUB1_DN_DP_1
- U12 pad 5: (no net) -> USB_VBUS_1
- U12 pad 6: (no net) -> HUB1_DN_DP_1
- U13 pad 1: (no net) -> MIC_VDD
- U13 pad 2: (no net) -> GND
- U13 pad 3: (no net) -> I2S_BCLK
- U13 pad 4: (no net) -> I2S_LRCLK
- U13 pad 5: (no net) -> I2S_DATA_IN
- U13 pad 6: (no net) -> GND
- U2 pad 1: (no net) -> 5V_SYS
- U2 pad 2: (no net) -> GND
- U2 pad 3: (no net) -> 5V_SYS
- U2 pad 4: (no net) -> NC
- U2 pad 5: (no net) -> 3V3_CLEAN
- U3 pad 1: (no net) -> 5V_SYS
- U3 pad 2: (no net) -> USB_UP_DP
- U3 pad 3: (no net) -> USB_UP_DM
- U3 pad 4: (no net) -> HUB1_VDD33
- U3 pad 5: (no net) -> HUB1_DN_DP_1
- U3 pad 6: (no net) -> HUB1_DN_DM_1
- U3 pad 7: (no net) -> HUB1_DN_DP_2
- U3 pad 8: (no net) -> HUB1_DN_DM_2
- U4 pad 1: (no net) -> 5V_SYS
- U4 pad 2: (no net) -> GND
- U4 pad 3: (no net) -> STINGER_EN_1
- U4 pad 4: (no net) -> USB_VBUS_1
- U4 pad 5: (no net) -> STINGER_ISET_1
- U5 pad 1: (no net) -> 5V_SYS
- U5 pad 2: (no net) -> GND
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
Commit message: feat: add NAU88C22 codec, ADS1115 ADC, SP3485 RS-485, TSOP38238 IR RX
New components (278 total, +31):
- NAU88C22 audio codec (QFN-32): full-duplex audio via TRRS jack,
  enables guitar pedal mode, headset mic, line-in. Shares I2S bus
  with INMP441 mics in TDM mode. I2C control at 0x1A.
- ADS1115 16-bit ADC (MSOP-10): 4 analog inputs on I2C1 (0x48),
  broken out to J17 header for sensors, expression pedals, 4-20mA.
- SP3485 RS-485 transceiver (SOIC-8): Modbus/DMX-512 on UART2
  (AUX_GPIO_1/2/3). 120ohm termination. J18 terminal header.
- TSOP38238 IR receiver: demodulated output to PCF8574 P7,
  completes IR subsystem (TX+RX). Learns any remote protocol.
- J19 UART debug header (1x4: GND/TX/RX/3V3)

Zero-cost fixes:
- MAX98357A GAIN_SLOT: GND→float = mono mix (L+R)/2 at +15dB
- IP5328P LIGHT pin: added amber LED for charge indication
- PCF8574 P7: GND→IR_RX (IR receiver output)
- TRRS Ring2: now wired to NAU88C22 codec LMICP (headset mic in)

Co-Authored-By: Claude Opus 4.6 (1M context) <noreply@anthropic.com>
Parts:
- added C105: 10u, C_0805_2012Metric, F.Cu at (232.0, 496.0)
- added C106: 100n, C_0402_1005Metric, F.Cu at (240.0, 496.0)
- added C107: 10u, C_0805_2012Metric, F.Cu at (248.0, 496.0)
- added C108: 100n, C_0402_1005Metric, F.Cu at (256.0, 496.0)
- added C109: 100u, CP_EIA-3528-21_Kemet-B, F.Cu at (264.0, 496.0)
- added C110: 100n, C_0402_1005Metric, F.Cu at (272.0, 496.0)
- added C111: 1u, C_0402_1005Metric, F.Cu at (280.0, 496.0)
- added C112: 1u, C_0402_1005Metric, F.Cu at (288.0, 496.0)
- added C113: 100u, CP_EIA-3528-21_Kemet-B, F.Cu at (216.0, 504.0)
- added C114: 100u, CP_EIA-3528-21_Kemet-B, F.Cu at (224.0, 504.0)
- added C115: 100n, C_0402_1005Metric, F.Cu at (248.0, 504.0)
- added C116: 100n, C_0402_1005Metric, F.Cu at (272.0, 504.0)
- added C117: 100n, C_0402_1005Metric, F.Cu at (288.0, 504.0)
- added C118: 4u7, C_0402_1005Metric, F.Cu at (200.0, 512.0)
- added FB3: BLM18AG601SN1, L_0603_1608Metric, F.Cu at (272.0, 370.0)
- added J17: Analog-In, PinHeader_1x04_P2.54mm_Vertical, F.Cu at (200.0, 280.0)
- added J18: RS485-Bus, PinHeader_1x03_P2.54mm_Vertical, F.Cu at (240.0, 280.0)
- added J19: UART-Debug, PinHeader_1x04_P2.54mm_Vertical, F.Cu at (280.0, 280.0)
- added LED9: AMBER_0402, LED_0402_1005Metric, F.Cu at (260.0, 370.0)
- added R56: 1k, R_0402_1005Metric, F.Cu at (224.0, 496.0)
- added R57: 10k, R_0402_1005Metric, F.Cu at (200.0, 504.0)
- added R58: 2.2k, R_0402_1005Metric, F.Cu at (208.0, 504.0)
- added R59: 0, R_0402_1005Metric, F.Cu at (232.0, 504.0)
- added R60: 10k, R_0402_1005Metric, F.Cu at (240.0, 504.0)
- added R61: 10k, R_0402_1005Metric, F.Cu at (256.0, 504.0)
- added R62: 120, R_0402_1005Metric, F.Cu at (264.0, 504.0)
- added R63: 100, R_0402_1005Metric, F.Cu at (280.0, 504.0)
- added U27: NAU88C22, QFN-32-1EP_5x5mm_P0.5mm_EP3.45x3.45mm, F.Cu at (260.0, 260.0)
- added U28: ADS1115, MSOP-10_3x3mm_P0.5mm, F.Cu at (280.0, 260.0)
- added U29: SP3485, SOIC-8_3.9x4.9mm_P1.27mm, F.Cu at (220.0, 280.0)
- added U30: TSOP38238, Vishay_MINICAST-3Pin, F.Cu at (260.0, 280.0)
- moved C1 20.0 mm to (200.0, 392.0)
- moved C10 20.0 mm to (280.0, 392.0)
- moved C100 20.0 mm to (264.0, 488.0)
- moved C101 20.0 mm to (272.0, 488.0)
- moved C102 20.0 mm to (280.0, 488.0)
- moved C103 20.0 mm to (288.0, 488.0)
- moved C104 20.0 mm to (200.0, 496.0)
- moved C11 20.0 mm to (288.0, 392.0)
- moved C12 20.0 mm to (200.0, 400.0)
- moved C13 20.0 mm to (240.0, 400.0)
- moved C14 20.0 mm to (288.0, 400.0)
- moved C15 20.0 mm to (200.0, 408.0)
- moved C16 20.0 mm to (208.0, 408.0)
- moved C17 20.0 mm to (216.0, 408.0)
- moved C18 20.0 mm to (240.0, 408.0)
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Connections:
- J15 pad R2: (no net) -> TRRS_RING2
- U10 pad 4: GND -> NC
- U21 pad 12: GND -> IR_RX

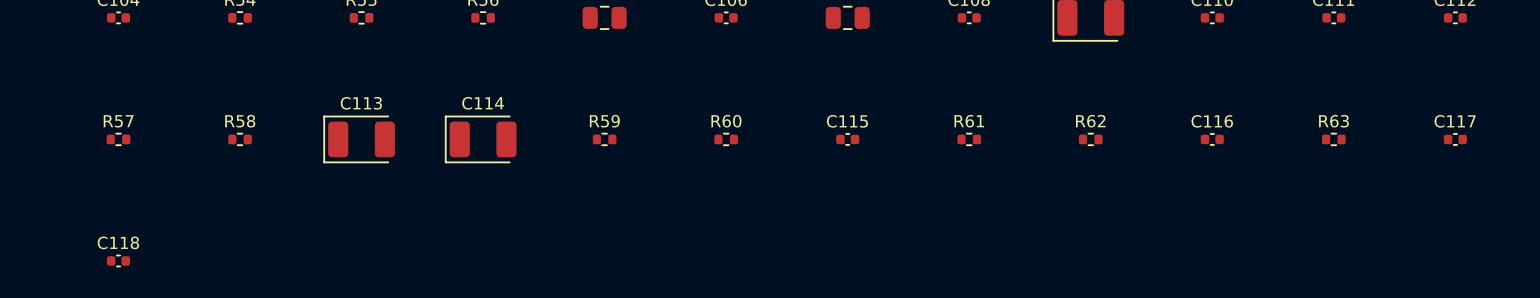
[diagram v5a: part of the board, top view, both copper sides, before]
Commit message: fix: audit findings — I2S bus fight, IR filter, LIGHT LED, RS485 boot
CRITICAL fixes:
- NAU88C22 ADCOUT: separate CODEC_ADCOUT net (was sharing I2S_DATA_IN
  with INMP441 mics = bus fight). Added 0R DNP jumper for optional
  connection when mics are disabled in firmware.
- TSOP38238: VCC filter was wired to IR_RX output instead of VS power
  pin. Created IR_VS_FILT net with proper 100R+100nF+4.7uF filtering.

WARNING fixes:
- IP5328P LIGHT LED: reversed polarity (open-drain sinks, can't source).
  Rewired as 3V3→1k→LED_A→LED_K→LIGHT pin.
- SP3485 RS485_DE: added 100k pull-down for default receive mode during
  boot before GPIO is configured.

280 components, 192 nets. All tests pass. KiCad re-imported.

Co-Authored-By: Claude Opus 4.6 (1M context) <noreply@anthropic.com>
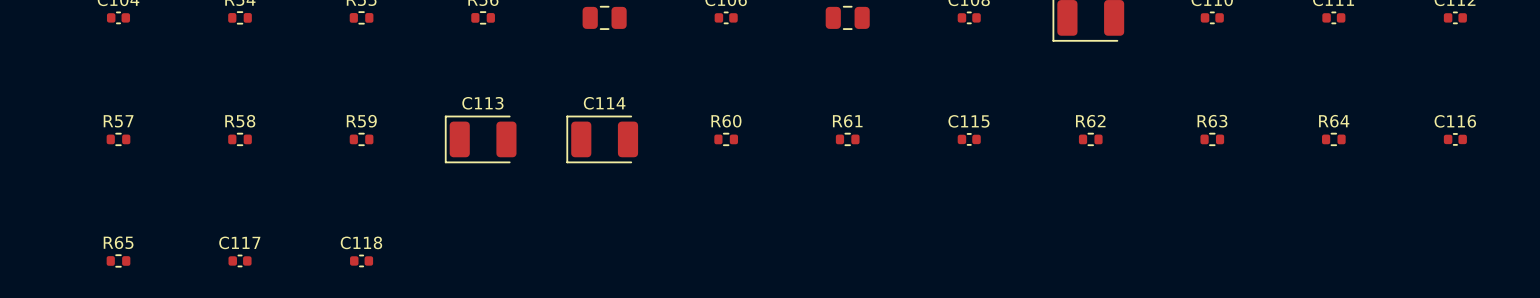
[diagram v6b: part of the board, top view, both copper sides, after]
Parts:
- added R64: 120, R_0402_1005Metric, F.Cu at (280.0, 504.0)
- added R65: 100, R_0402_1005Metric, F.Cu at (200.0, 512.0)
- R58: value 2.2k -> 0R_DNP
- R59: value 0 -> 2.2k
- R60: value 10k -> 0
- R62: value 120 -> 10k
- R63: value 100 -> 100k
- moved C117 80.4 mm to (208.0, 512.0)
- moved C116 16.0 mm to (288.0, 504.0)
- moved C118 16.0 mm to (216.0, 512.0)
- moved R59 16.0 mm to (216.0, 504.0)
- moved C113 8.00 mm to (224.0, 504.0)
- moved C114 8.00 mm to (232.0, 504.0)
- moved C115 8.00 mm to (256.0, 504.0)
- moved R61 8.00 mm to (248.0, 504.0)
- moved R63 8.00 mm to (272.0, 504.0)
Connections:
- C117 pad 1: 3V3_SYS -> IR_VS_FILT
- C118 pad 1: 3V3_SYS -> IR_VS_FILT
- LED9 pad 1: GND -> IP5328P_LIGHT
- R56 pad 1: IP5328P_LIGHT -> 3V3_SYS
- R58 pad 1: CODEC_MICBIAS -> CODEC_ADCOUT
- R58 pad 2: TRRS_RING2 -> I2S_DATA_IN
- R59 pad 1: ADC_ADDR -> CODEC_MICBIAS
- R59 pad 2: GND -> TRRS_RING2
- R60 pad 1: 3V3_SYS -> ADC_ADDR
- R60 pad 2: ADC_ALRT -> GND
- R61 pad 1: AUX_GPIO_3 -> 3V3_SYS
- R61 pad 2: RS485_DE -> ADC_ALRT
- R62 pad 1: RS485_A -> AUX_GPIO_3
- R62 pad 2: RS485_B -> RS485_DE
- R63 pad 1: 3V3_SYS -> RS485_DE
- R63 pad 2: IR_RX -> GND
- U27 pad 24: I2S_DATA_IN -> CODEC_ADCOUT
- U30 pad 3: 3V3_SYS -> IR_VS_FILT
